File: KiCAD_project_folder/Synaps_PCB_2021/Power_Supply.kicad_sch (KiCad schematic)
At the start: 16 parts, among them J1 USB_C_Receptacle, U1 MAX77680AEWV+

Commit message: Added library for one piece
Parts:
- removed U1: MAX77680AEWV+, 21-100047A_W302H2+1_MXM, symbol 2021-11-05_01-01-14:MAX77680AEWV+
- added U1: MAX77680AEWV+, 21-100047A_W302H2+1_MXM, symbol MAX77680AEWV+:MAX77680AEWV+
- renumbered C4 to C1, C59 to C2, C9 to C3, C5 to C4, C10 to C5, R6 to R1, R7 to R2, R8 to R3
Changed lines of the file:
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@@
     (effects (font (size 1.27 1.27)) (justify right))
   )
-  (symbol (lib_id "Connector:USB_C_Receptacle") (at 34.29 54.61 0)
+  (symbol (lib_id "Connector:USB_C_Receptacle") (at 34.29 54.61 0) (unit 1)
     (in_bom yes) (on_board yes)
     (property "Reference" "J1" (id 0) (at 37.0078 22.4282 0))
@@
   (symbol (lib_id "power:GNDREF") (at 26.67 99.06 0) (unit 1)
     (in_bom yes) (on_board yes)
-    (property "Reference" "#PWR06" (id 0) (at 26.67 105.41 0)
+    (property "Reference" "#PWR01" (id 0) (at 26.67 105.41 0)
       (effects (font (size 1.27 1.27)) hide)
     )
@@
   (symbol (lib_id "power:GNDREF") (at 34.29 99.06 0) (unit 1)
     (in_bom yes) (on_board yes)
-    (property "Reference" "#PWR019" (id 0) (at 34.29 105.41 0)
+    (property "Reference" "#PWR02" (id 0) (at 34.29 105.41 0)
       (effects (font (size 1.27 1.27)) hide)
     )
@@
   (symbol (lib_id "power:GNDREF") (at 204.47 49.53 180) (unit 1)
     (in_bom yes) (on_board yes)
-    (property "Reference" "#PWR09" (id 0) (at 204.47 43.18 0)
+    (property "Reference" "#PWR08" (id 0) (at 204.47 43.18 0)
       (effects (font (size 1.27 1.27)) hide)
     )
@@
   (symbol (lib_id "power:GNDREF") (at 204.47 62.23 0) (unit 1)
     (in_bom yes) (on_board yes)
-    (property "Reference" "#PWR010" (id 0) (at 204.47 68.58 0)
+    (property "Reference" "#PWR09" (id 0) (at 204.47 68.58 0)
       (effects (font (size 1.27 1.27)) hide)
     )
@@
   (symbol (lib_id "power:GNDREF") (at 213.36 62.23 0) (unit 1)
     (in_bom yes) (on_board yes)
-    (property "Reference" "#PWR011" (id 0) (at 213.36 68.58 0)
+    (property "Reference" "#PWR010" (id 0) (at 213.36 68.58 0)
       (effects (font (size 1.27 1.27)) hide)
     )
@@
   (symbol (lib_id "Device:C_Small") (at 120.65 80.01 0) (unit 1)
     (in_bom yes) (on_board yes)
-    (property "Reference" "C4" (id 0) (at 116.84 77.47 0)
+    (property "Reference" "C1" (id 0) (at 116.84 77.47 0)
       (effects (font (size 1.27 1.27)) (justify left))
     )
@@
   (symbol (lib_id "power:GNDREF") (at 120.65 87.63 0) (unit 1)
     (in_bom yes) (on_board yes)
-    (property "Reference" "#PWR07" (id 0) (at 120.65 93.98 0)
+    (property "Reference" "#PWR03" (id 0) (at 120.65 93.98 0)
       (effects (font (size 1.27 1.27)) hide)
     )
@@
   (symbol (lib_id "Device:C_Small") (at 195.58 46.99 0) (unit 1)
     (in_bom yes) (on_board yes)
-    (property "Reference" "C5" (id 0) (at 191.77 44.45 0)
+    (property "Reference" "C4" (id 0) (at 191.77 44.45 0)
       (effects (font (size 1.27 1.27)) (justify left))
     )
@@
   (symbol (lib_id "Device:C_Small") (at 187.96 67.31 180) (unit 1)
     (in_bom yes) (on_board yes)
-    (property "Reference" "C9" (id 0) (at 187.96 66.04 0)
+    (property "Reference" "C3" (id 0) (at 187.96 66.04 0)
       (effects (font (size 1.27 1.27)) (justify right))
     )
@@
   (symbol (lib_id "Device:C_Small") (at 195.58 77.47 0) (unit 1)
     (in_bom yes) (on_board yes)
-    (property "Reference" "C10" (id 0) (at 198.12 76.2 0)
+    (property "Reference" "C5" (id 0) (at 198.12 76.2 0)
       (effects (font (size 1.27 1.27)) (justify left))
     )
@@
   (symbol (lib_id "power:GNDREF") (at 195.58 82.55 0) (unit 1)
     (in_bom yes) (on_board yes)
-    (property "Reference" "#PWR012" (id 0) (at 195.58 88.9 0)
+    (property "Reference" "#PWR07" (id 0) (at 195.58 88.9 0)
       (effects (font (size 1.27 1.27)) hide)
     )
@@
   (symbol (lib_id "Device:C_Small") (at 185.42 91.44 0) (unit 1)
     (in_bom yes) (on_board yes)
-    (property "Reference" "C59" (id 0) (at 187.96 90.17 0)
+    (property "Reference" "C2" (id 0) (at 187.96 90.17 0)
       (effects (font (size 1.27 1.27)) (justify left))
     )
@@
   (symbol (lib_id "power:GNDREF") (at 185.42 96.52 0) (unit 1)
     (in_bom yes) (on_board yes)
-    (property "Reference" "#PWR014" (id 0) (at 185.42 102.87 0)
+    (property "Reference" "#PWR06" (id 0) (at 185.42 102.87 0)
       (effects (font (size 1.27 1.27)) hide)
     )
@@
   (symbol (lib_id "power:VDD") (at 124.46 41.91 0) (unit 1)
     (in_bom yes) (on_board yes)
-    (property "Reference" "#PWR013" (id 0) (at 124.46 45.72 0)
+    (property "Reference" "#PWR04" (id 0) (at 124.46 45.72 0)
       (effects (font (size 1.27 1.27)) hide)
     )
@@
   (symbol (lib_id "Device:R_US") (at 119.38 55.88 0) (unit 1)
     (in_bom yes) (on_board yes)
-    (property "Reference" "R6" (id 0) (at 113.03 53.34 0)
+    (property "Reference" "R1" (id 0) (at 113.03 53.34 0)
       (effects (font (size 1.27 1.27)) (justify left))
     )
@@
   (symbol (lib_id "Device:R_US") (at 128.27 53.34 0) (unit 1)
     (in_bom yes) (on_board yes)
-    (property "Reference" "R8" (id 0) (at 121.92 52.07 0)
+    (property "Reference" "R3" (id 0) (at 121.92 52.07 0)
       (effects (font (size 1.27 1.27)) (justify left))
     )
@@
   (symbol (lib_id "Device:R_US") (at 125.73 102.87 0) (unit 1)
     (in_bom yes) (on_board yes)
-    (property "Reference" "R7" (id 0) (at 127.4572 101.7016 0)
+    (property "Reference" "R2" (id 0) (at 127.4572 101.7016 0)
       (effects (font (size 1.27 1.27)) (justify left))
     )
@@
   (symbol (lib_id "power:GNDREF") (at 125.73 106.68 0) (unit 1)
     (in_bom yes) (on_board yes)
-    (property "Reference" "#PWR08" (id 0) (at 125.73 113.03 0)
+    (property "Reference" "#PWR05" (id 0) (at 125.73 113.03 0)
       (effects (font (size 1.27 1.27)) hide)
     )
@@
     (pin "1")
   )
-  (symbol (lib_id "2021-11-05_01-01-14:MAX77680AEWV+") (at 115.57 151.13 0) (unit 1)
-    (in_bom yes) (on_board yes)
-    (property "Reference" "U1" (id 0) (at 140.97 141.3002 0)
+  (symbol (lib_id "MAX77680AEWV+:MAX77680AEWV+") (at 35.56 134.62 0) (unit 1)
+    (in_bom yes) (on_board yes) (fields_autoplaced)
+    (property "Reference" "U1" (id 0) (at 60.96 125.3924 0)
       (effects (font (size 1.524 1.524)))
     )
-    (property "Value" "MAX77680AEWV+" (id 1) (at 140.97 143.9926 0)
+    (property "Value" "MAX77680AEWV+" (id 1) (at 60.96 128.3858 0)
       (effects (font (size 1.524 1.524)))
     )
-    (property "Footprint" "21-100047A_W302H2+1_MXM" (id 2) (at 140.97 145.034 0)
+    (property "Footprint" "21-100047A_W302H2+1_MXM" (id 2) (at 60.96 128.524 0)
       (effects (font (size 1.524 1.524)) hide)
     )
-    (property "Datasheet" "" (id 3) (at 115.57 151.13 0)
+    (property "Datasheet" "" (id 3) (at 35.56 134.62 0)
       (effects (font (size 1.524 1.524)))
     )
+    (pin "A1")
+    (pin "A2")
+    (pin "A3")
+    (pin "A4")
+    (pin "A5")
+    (pin "A6")
+    (pin "B1")
+    (pin "B2")
+    (pin "B3")
+    (pin "B4")
+    (pin "B5")
+    (pin "B6")
+    (pin "C1")
+    (pin "C2")
+    (pin "C3")
+    (pin "C4")
+    (pin "C5")
+    (pin "C6")
+    (pin "D1")
+    (pin "D2")
+    (pin "D3")
+    (pin "D4")
+    (pin "D5")
+    (pin "D6")
+    (pin "E1")
+    (pin "E2")
+    (pin "E3")
+    (pin "E4")
+    (pin "E5")
+    (pin "E6")
   )
 )

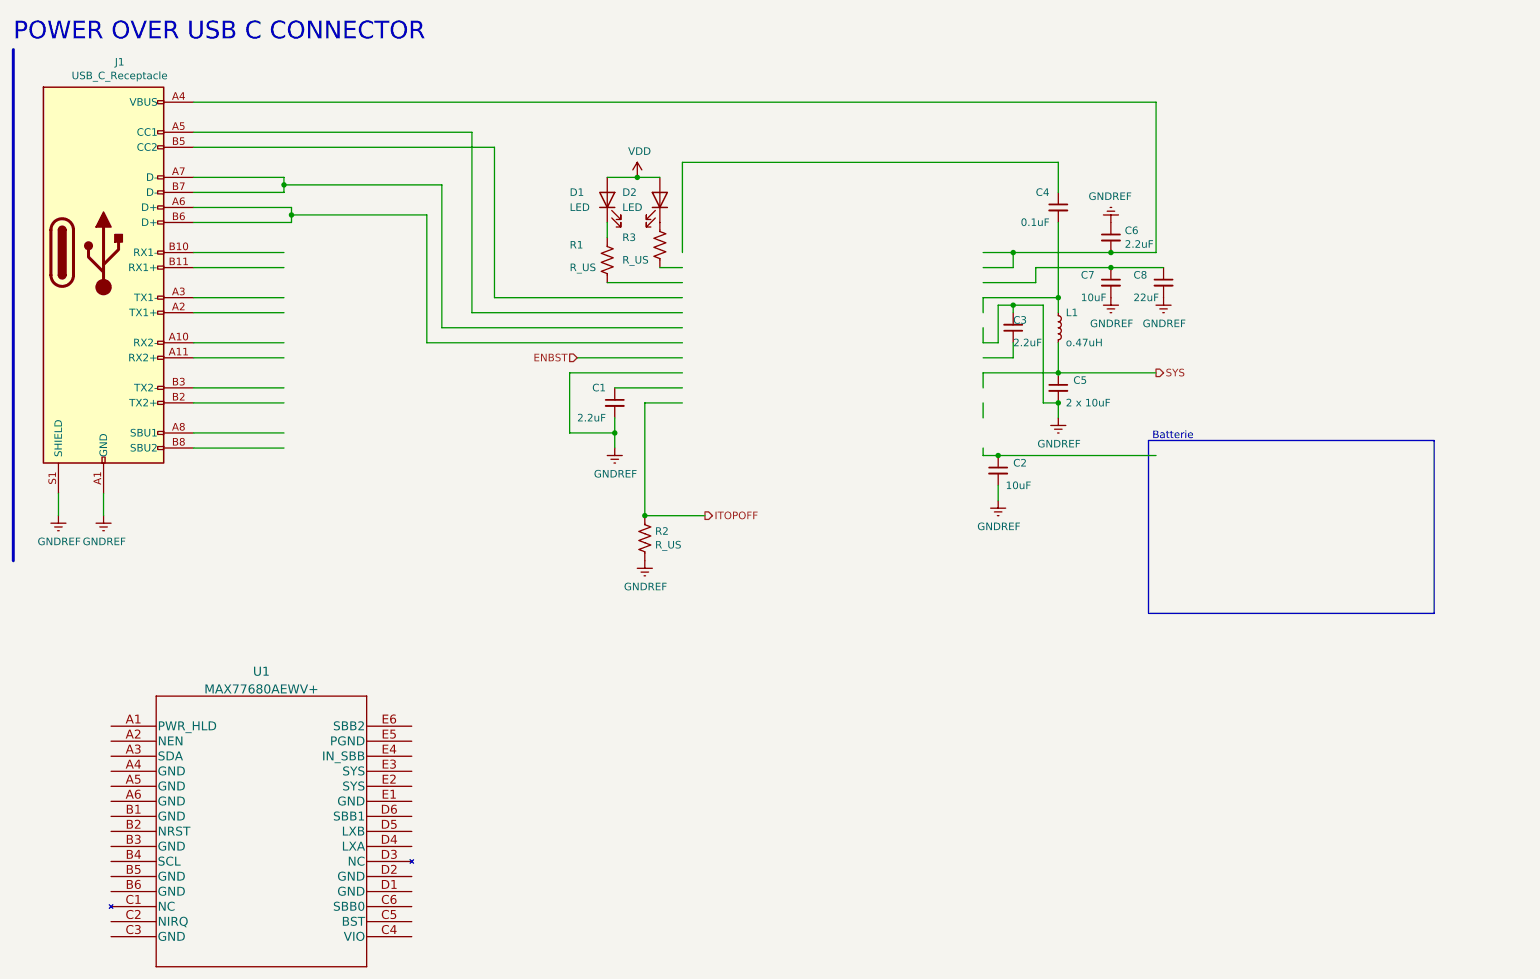
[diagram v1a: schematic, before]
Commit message: Added new library and changement de power ic, old one unavailable
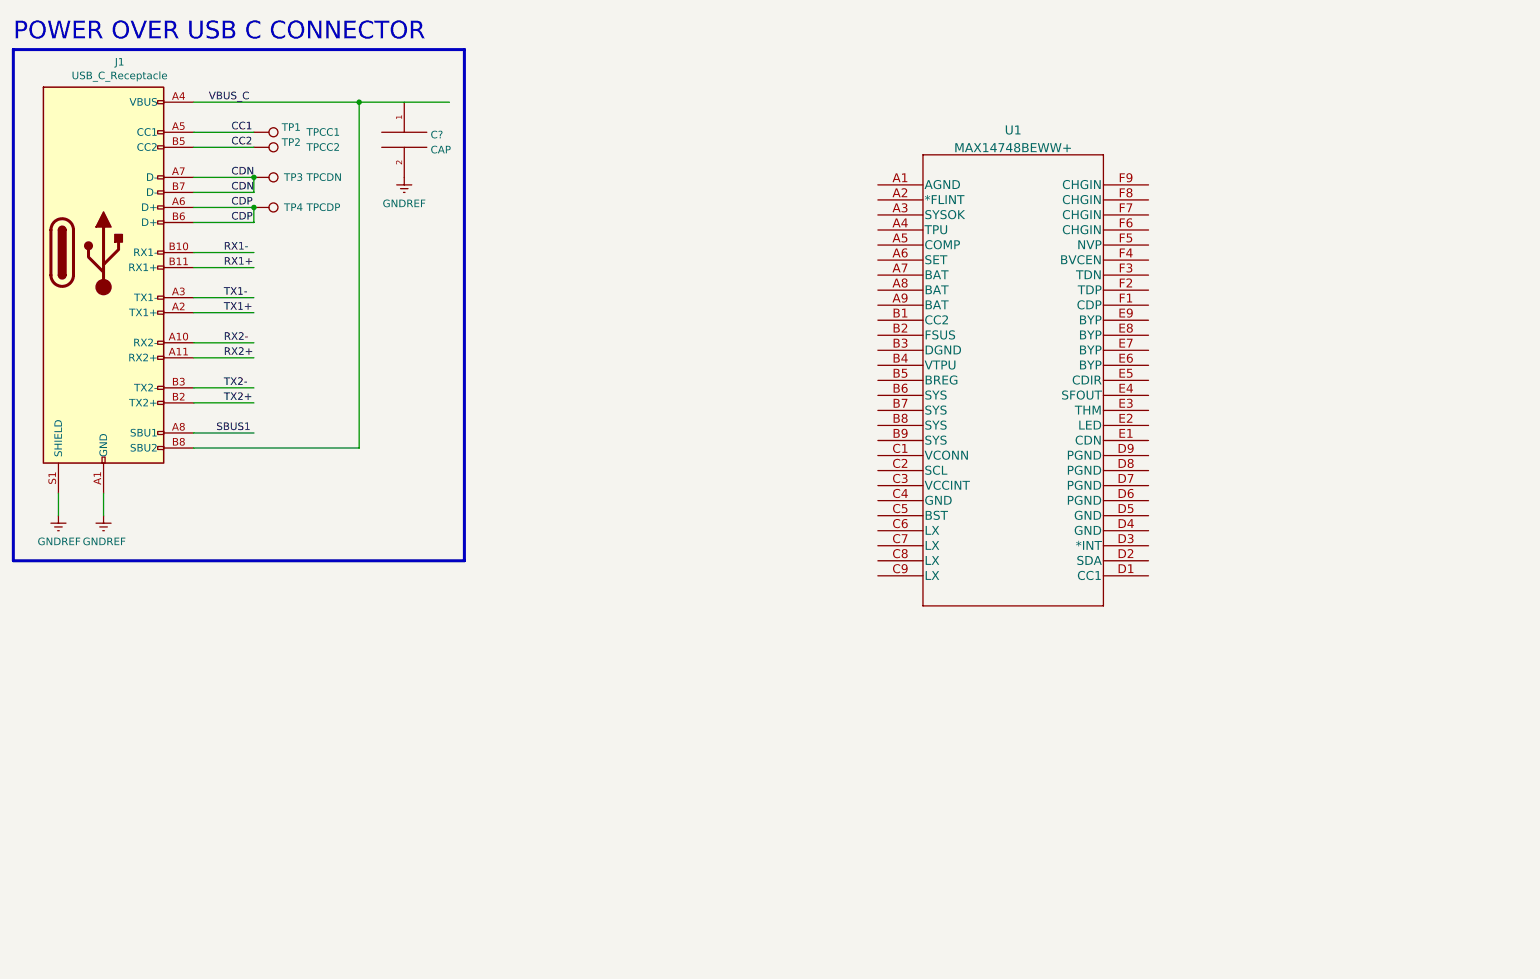
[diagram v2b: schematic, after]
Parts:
- removed C1, C3, C6: 2.2uF, symbol Device:C_Small
- removed C2, C7: 10uF, symbol Device:C_Small
- removed C4: 0.1uF, symbol Device:C_Small
- removed C5: 2 x 10uF, symbol Device:C_Small
- removed C8: 22uF, symbol Device:C_Small
- removed D1, D2: LED, symbol Device:LED
- removed L1: o.47uH, symbol Device:L_Small
- removed R1, R2, R3: R_US, symbol Device:R_US
- removed U1: MAX77680AEWV+, 21-100047A_W302H2+1_MXM, symbol MAX77680AEWV+:MAX77680AEWV+
- added C?: CAP, symbol pspice:CAP
- added TP1: TPCC1, symbol Connector:TestPoint
- added TP2: TPCC2, symbol Connector:TestPoint
- added TP3: TPCDN, symbol Connector:TestPoint
- added TP4: TPCDP, symbol Connector:TestPoint
- added U1: MAX14748BEWW+, 21-100122_W542C3+1_MXM, symbol MAX14748:MAX14748BEWW+
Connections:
- net GNDREF: now also C?.2
- net RX2-: now reaches J1.A10 (RX2-)
- net RX2+: now reaches J1.A11 (RX2+)
- net TX1+: now reaches J1.A2 (TX1+)
- net TX1-: now reaches J1.A3 (TX1-)
- net VBUS_C: now reaches J1.A4 (VBUS), J1.A9 (VBUS), J1.B4 (VBUS), J1.B9 (VBUS)
- net VBUS_C: now also J1.B8 (SBU2)
- net CC1: now reaches J1.A5 (CC1)
- net CC1: now also TP1.1
- net CDP: now reaches J1.A6 (D+), J1.B6 (D+)
- net CDP: now also TP4.1
- net CDN: now reaches J1.A7 (D-), J1.B7 (D-)
- net CDN: now also TP3.1
- net SBUS1: now reaches J1.A8 (SBU1)
- net RX1-: now reaches J1.B10 (RX1-)
- net RX1+: now reaches J1.B11 (RX1+)
- net TX2+: now reaches J1.B2 (TX2+)
- net TX2-: now reaches J1.B3 (TX2-)
- net CC2: now reaches J1.B5 (CC2)
- net CC2: now also TP2.1
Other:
- note removed: "Batterie"

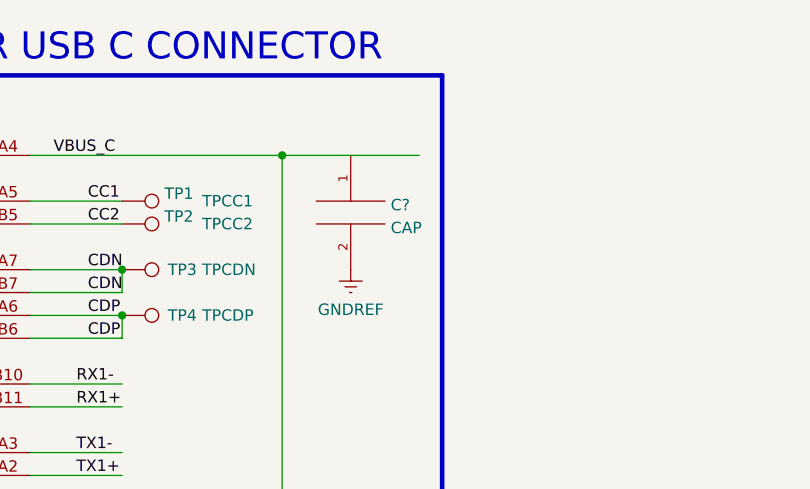
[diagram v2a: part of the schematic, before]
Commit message: Added LTC2452 librairy
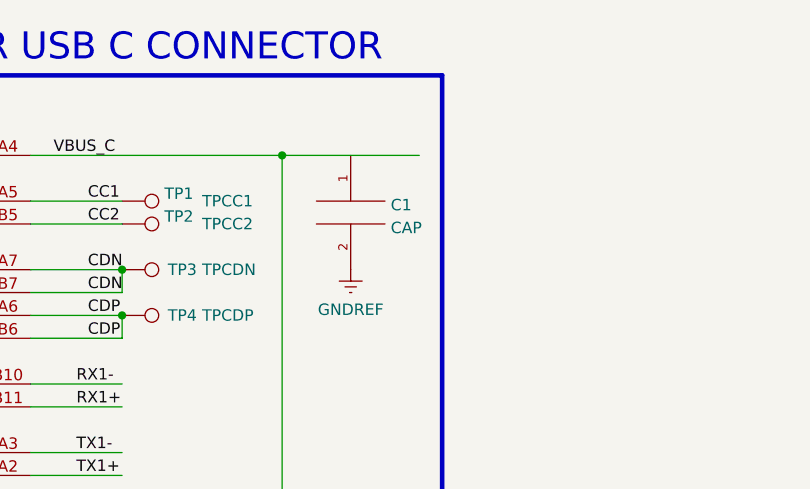
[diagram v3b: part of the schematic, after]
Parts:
- gave numbers to parts that had none: 1
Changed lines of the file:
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@@
   (symbol (lib_id "power:GNDREF") (at 85.09 41.91 0) (unit 1)
     (in_bom yes) (on_board yes) (fields_autoplaced)
-    (property "Reference" "#PWR?" (id 0) (at 85.09 48.26 0)
+    (property "Reference" "#PWR03" (id 0) (at 85.09 48.26 0)
       (effects (font (size 1.27 1.27)) hide)
     )
@@
   (symbol (lib_id "pspice:CAP") (at 85.09 35.56 0) (unit 1)
     (in_bom yes) (on_board yes) (fields_autoplaced)
-    (property "Reference" "C?" (id 0) (at 89.535 34.7253 0)
+    (property "Reference" "C1" (id 0) (at 89.535 34.7253 0)
       (effects (font (size 1.27 1.27)) (justify left))
     )

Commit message: Added basic PCB guidelines
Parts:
- C1: footprint (none) -> Capacitor_SMD:C_1206_3216Metric_Pad1.33x1.80mm_HandSolder
- J1: footprint (none) -> Connector_USB:USB_C_Receptacle_HRO_TYPE-C-31-M-12
- TP1, TP2, TP3, TP4: footprint (none) -> TestPoint:TestPoint_Pad_D1.0mm
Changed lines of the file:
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@@
     (property "Reference" "J1" (id 0) (at 37.0078 22.4282 0))
     (property "Value" "USB_C_Receptacle" (id 1) (at 37.0078 24.7396 0))
-    (property "Footprint" "" (id 2) (at 38.1 54.61 0)
+    (property "Footprint" "Connector_USB:USB_C_Receptacle_HRO_TYPE-C-31-M-12" (id 2) (at 38.1 54.61 0)
       (effects (font (size 1.27 1.27)) hide)
     )
@@
       (effects (font (size 1.27 1.27)) (justify left))
     )
-    (property "Footprint" "" (id 2) (at 59.69 41.91 0)
+    (property "Footprint" "TestPoint:TestPoint_Pad_D1.0mm" (id 2) (at 59.69 41.91 0)
       (effects (font (size 1.27 1.27)) hide)
     )
@@
       (effects (font (size 1.27 1.27)) (justify left))
     )
-    (property "Footprint" "" (id 2) (at 59.69 39.37 0)
+    (property "Footprint" "TestPoint:TestPoint_Pad_D1.0mm" (id 2) (at 59.69 39.37 0)
       (effects (font (size 1.27 1.27)) hide)
     )
@@
       (effects (font (size 1.27 1.27)) (justify left))
     )
-    (property "Footprint" "" (id 2) (at 59.69 52.07 0)
+    (property "Footprint" "TestPoint:TestPoint_Pad_D1.0mm" (id 2) (at 59.69 52.07 0)
       (effects (font (size 1.27 1.27)) hide)
     )
@@
       (effects (font (size 1.27 1.27)) (justify left))
     )
-    (property "Footprint" "" (id 2) (at 85.09 35.56 0)
+    (property "Footprint" "Capacitor_SMD:C_1206_3216Metric_Pad1.33x1.80mm_HandSolder" (id 2) (at 85.09 35.56 0)
       (effects (font (size 1.27 1.27)) hide)
     )
@@
       (effects (font (size 1.27 1.27)) (justify left))
     )
-    (property "Footprint" "" (id 2) (at 59.69 46.99 0)
-      (effects (font (size 1.27 1.27)) hide)
-    )
+    (property "Footprint" "TestPoint:TestPoint_Pad_D1.0mm" (id 2) (at 59.69 46.99 0)
+      (effects (font (size 1.27 1.27)) hide)
+    )
